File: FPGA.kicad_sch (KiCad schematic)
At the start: 39 parts, among them U3A LFE5U-25F-8MG285C, U3B LFE5U-25F-8MG285C, U3C LFE5U-25F-8MG285C, U3D LFE5U-25F-8MG285C, U3E LFE5U-25F-8MG285C, U3F LFE5U-25F-8MG285C, U3G LFE5U-25F-8MG285C, U3H LFE5U-25F-8MG285C, U3I LFE5U-25F-8MG285C, U6 W25Q128JVP

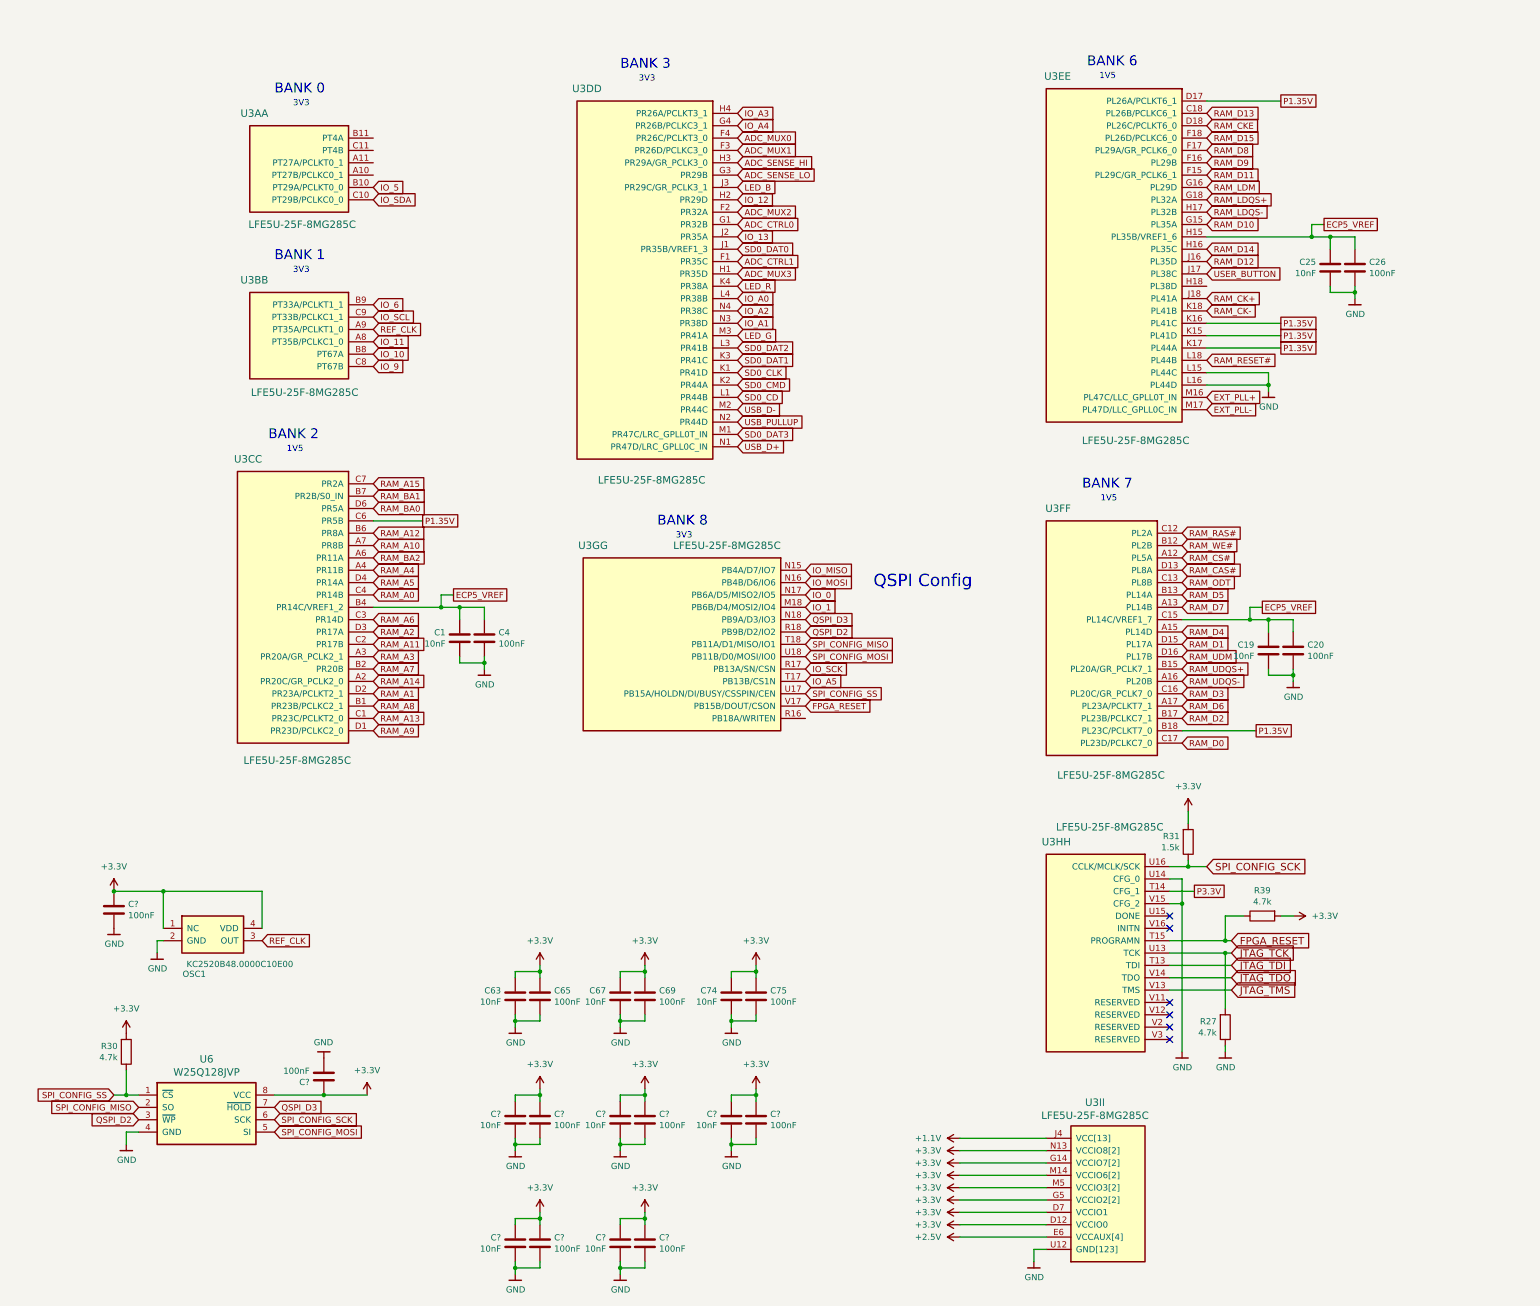
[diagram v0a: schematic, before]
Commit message: split fpga into two sheet. Connect jtag signals.
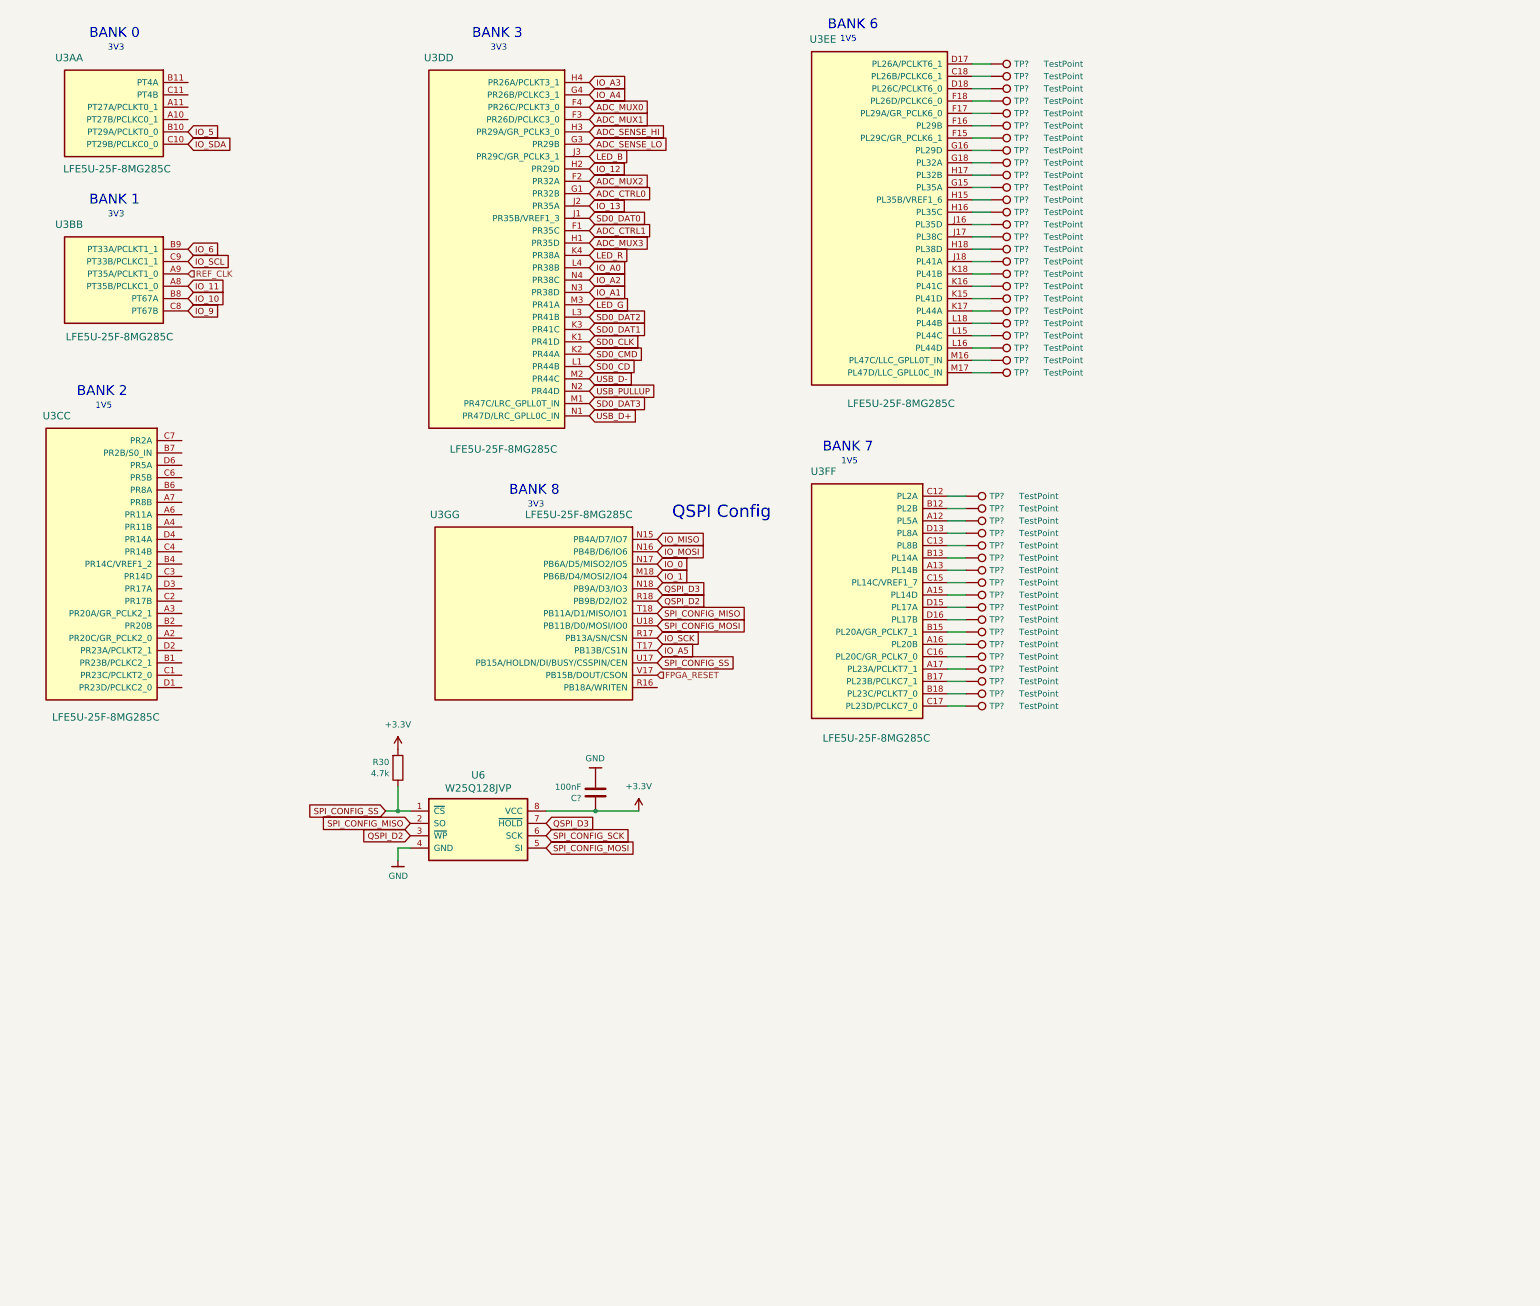
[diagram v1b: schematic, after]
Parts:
- removed C1, C19, C25, C63, C67, C74, C? (x5): 10nF, gkl_dipol:C_0201_0603Metric, symbol Device:C
- removed C20, C26, C4, C65, C69, C75, C? (x7): 100nF, gkl_dipol:C_0201_0603Metric, symbol Device:C
- removed OSC1: KC2520B48.0000C10E00, gkl_time:Oscilator_2.5x2.0, symbol gkl_time:TYETBCSANF-32.000000
- removed R27, R39: 4.7k, gkl_dipol:R_0201_0603Metric, symbol Device:R
- removed R31: 1.5k, gkl_dipol:R_0201_0603Metric, symbol Device:R
- removed U3H, U3I: LFE5U-25F-8MG285C, gkl_housings_bga:csBGA285, symbol gkl_lattice:ECP5U25-MG285
- added C?: 100nF, gkl_dipol:C_0201_0603Metric, symbol Device:C
- added TP? (x44): TestPoint, symbol Connector:TestPoint
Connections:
- net +3.3V: now also C?.1
- net GND: now also C?.2; no longer U3E.L15 (PL44C), U3E.L16 (PL44D)
- net at U3E.H18 (PL38D): now also TP?.1
- removed net ECP5_VREF: U3C.B4 (PR14C/VREF1_2), U3E.H15 (PL35B/VREF1_6), U3F.C15 (PL14C/VREF1_7)
- net EXT_PLL+: no longer names the net of U3E.M16 (PL47C/LLC_GPLL0T_IN)
- net EXT_PLL+: now also TP?.1
- net EXT_PLL-: no longer names the net of U3E.M17 (PL47D/LLC_GPLL0C_IN)
- net EXT_PLL-: now also TP?.1
- removed net P1.35V: U3C.C6 (PR5B), U3E.D17 (PL26A/PCLKT6_1), U3E.K15 (PL41D), U3E.K16 (PL41C), U3E.K17 (PL44A), U3F.B18 (PL23C/PCLKT7_0)
- net RAM_A0: no longer names the net of U3C.C4 (PR14B)
- net RAM_A1: no longer names the net of U3C.D2 (PR23A/PCLKT2_1)
- net RAM_A10: no longer names the net of U3C.A7 (PR8B)
- net RAM_A11: no longer names the net of U3C.C2 (PR17B)
- net RAM_A12: no longer names the net of U3C.B6 (PR8A)
- net RAM_A13: no longer names the net of U3C.C1 (PR23C/PCLKT2_0)
- net RAM_A14: no longer names the net of U3C.A2 (PR20C/GR_PCLK2_0)
- net RAM_A15: no longer names the net of U3C.C7 (PR2A)
- net RAM_A2: no longer names the net of U3C.D3 (PR17A)
- net RAM_A3: no longer names the net of U3C.A3 (PR20A/GR_PCLK2_1)
- net RAM_A4: no longer names the net of U3C.A4 (PR11B)
- net RAM_A5: no longer names the net of U3C.D4 (PR14A)
- net RAM_A6: no longer names the net of U3C.C3 (PR14D)
- net RAM_A7: no longer names the net of U3C.B2 (PR20B)
- net RAM_A8: no longer names the net of U3C.B1 (PR23B/PCLKC2_1)
- net RAM_A9: no longer names the net of U3C.D1 (PR23D/PCLKC2_0)
- net RAM_BA0: no longer names the net of U3C.D6 (PR5A)
- net RAM_BA1: no longer names the net of U3C.B7 (PR2B/S0_IN)
- net RAM_BA2: no longer names the net of U3C.A6 (PR11A)
- net RAM_CAS#: no longer names the net of U3F.D13 (PL8A)
- net RAM_CAS#: now also TP?.1
- net RAM_CK+: no longer names the net of U3E.J18 (PL41A)
- net RAM_CK+: now also TP?.1
- net RAM_CK-: no longer names the net of U3E.K18 (PL41B)
- net RAM_CK-: now also TP?.1
- net RAM_CKE: no longer names the net of U3E.D18 (PL26C/PCLKT6_0)
- net RAM_CKE: now also TP?.1
- net RAM_CS#: no longer names the net of U3F.A12 (PL5A)
- net RAM_CS#: now also TP?.1
- net RAM_D0: no longer names the net of U3F.C17 (PL23D/PCLKC7_0)
- net RAM_D0: now also TP?.1
- net RAM_D1: no longer names the net of U3F.D15 (PL17A)
- net RAM_D1: now also TP?.1
- net RAM_D10: no longer names the net of U3E.G15 (PL35A)
- net RAM_D10: now also TP?.1
- net RAM_D11: no longer names the net of U3E.F15 (PL29C/GR_PCLK6_1)
- net RAM_D11: now also TP?.1
- net RAM_D12: no longer names the net of U3E.J16 (PL35D)
- net RAM_D12: now also TP?.1
- net RAM_D13: no longer names the net of U3E.C18 (PL26B/PCLKC6_1)
- net RAM_D13: now also TP?.1
- net RAM_D14: no longer names the net of U3E.H16 (PL35C)
- net RAM_D14: now also TP?.1
- net RAM_D15: no longer names the net of U3E.F18 (PL26D/PCLKC6_0)
- net RAM_D15: now also TP?.1
- net RAM_D2: no longer names the net of U3F.B17 (PL23B/PCLKC7_1)
- net RAM_D2: now also TP?.1
- net RAM_D3: no longer names the net of U3F.C16 (PL20C/GR_PCLK7_0)
- net RAM_D3: now also TP?.1
- net RAM_D4: no longer names the net of U3F.A15 (PL14D)
- net RAM_D4: now also TP?.1
- net RAM_D5: no longer names the net of U3F.B13 (PL14A)
- net RAM_D5: now also TP?.1
- net RAM_D6: no longer names the net of U3F.A17 (PL23A/PCLKT7_1)
- net RAM_D6: now also TP?.1
- net RAM_D7: no longer names the net of U3F.A13 (PL14B)
- net RAM_D7: now also TP?.1
- net RAM_D8: no longer names the net of U3E.F17 (PL29A/GR_PCLK6_0)
- net RAM_D8: now also TP?.1
- net RAM_D9: no longer names the net of U3E.F16 (PL29B)
- net RAM_D9: now also TP?.1
- net RAM_LDM: no longer names the net of U3E.G16 (PL29D)
- net RAM_LDM: now also TP?.1
- net RAM_LDQS+: no longer names the net of U3E.G18 (PL32A)
- net RAM_LDQS+: now also TP?.1
- net RAM_LDQS-: no longer names the net of U3E.H17 (PL32B)
- net RAM_LDQS-: now also TP?.1
- net RAM_ODT: no longer names the net of U3F.C13 (PL8B)
- net RAM_ODT: now also TP?.1
- net RAM_RAS#: no longer names the net of U3F.C12 (PL2A)
- net RAM_RAS#: now also TP?.1
- net RAM_RESET#: no longer names the net of U3E.L18 (PL44B)
- net RAM_RESET#: now also TP?.1
- net RAM_UDM: no longer names the net of U3F.D16 (PL17B)
- net RAM_UDM: now also TP?.1
- net RAM_UDQS+: no longer names the net of U3F.B15 (PL20A/GR_PCLK7_1)
- net RAM_UDQS+: now also TP?.1
- net RAM_UDQS-: no longer names the net of U3F.A16 (PL20B)
- net RAM_UDQS-: now also TP?.1
- net RAM_WE#: no longer names the net of U3F.B12 (PL2B)
- net RAM_WE#: now also TP?.1
- net USER_BUTTON: no longer names the net of U3E.J17 (PL38C)
- net USER_BUTTON: now also TP?.1
- new net: TP?.1, U3E.D17 (PL26A/PCLKT6_1)
- new net: TP?.1, U3E.H15 (PL35B/VREF1_6)
- new net: TP?.1, U3E.K15 (PL41D)
- new net: TP?.1, U3E.K16 (PL41C)
- new net: TP?.1, U3E.K17 (PL44A)
- new net: TP?.1, U3E.L15 (PL44C)
- new net: TP?.1, U3E.L16 (PL44D)
- new net: TP?.1, U3F.B18 (PL23C/PCLKT7_0)
- new net: TP?.1, U3F.C15 (PL14C/VREF1_7)
- no-connect marks 6 -> 0
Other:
- title: FPGA -> FPGALER 
- moved on the sheet: R30, U3AA, U3BB, U3CC, U3DD, U3EE, U3FF, U3GG, U6
